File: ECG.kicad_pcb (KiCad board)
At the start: 2 copper layers, 50 x 50 mm, 84 parts, among them J1 SJ-3566AN, J2 Conn_01x02_Male, Q1 MMBT3904-7-F, U1 ADR4525, U2 SP6641, U3 INA333, U4 OPA388, U5 OPA388, U6 OPA388, U7 ADS1015IDGS

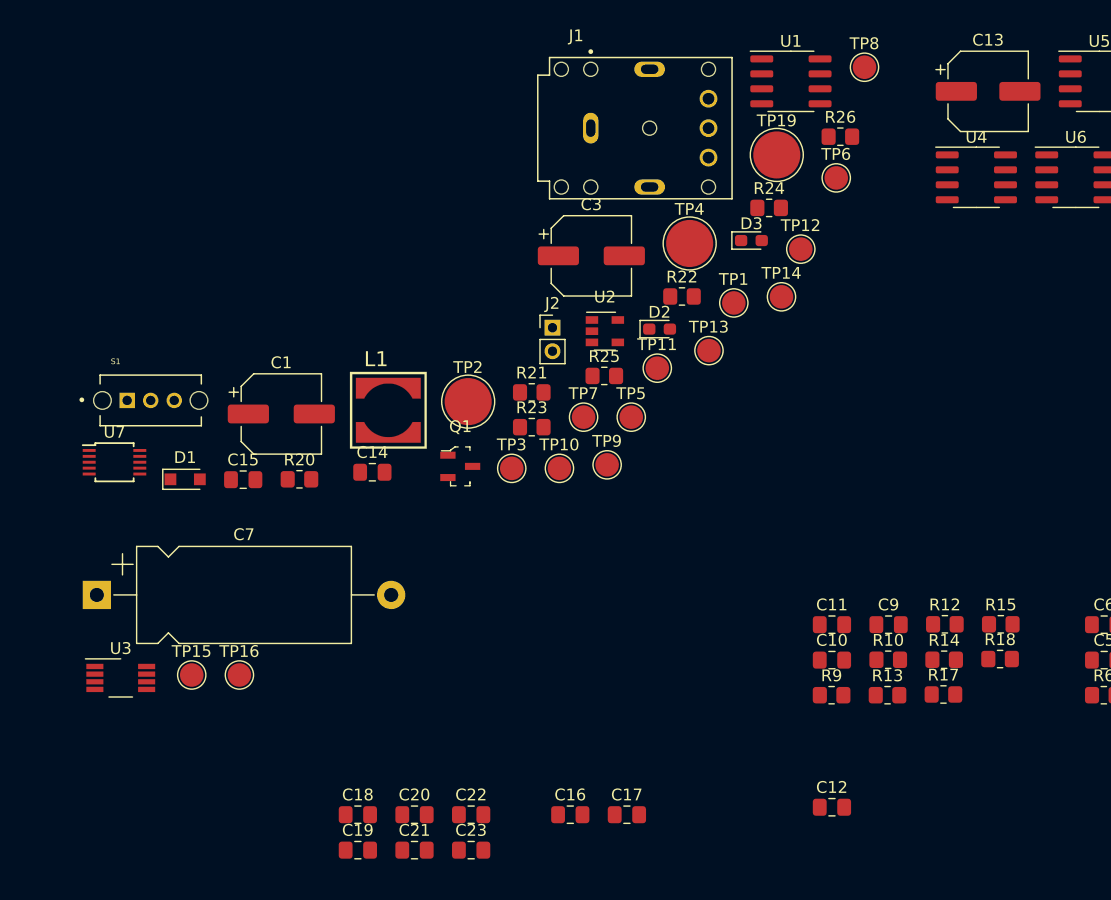
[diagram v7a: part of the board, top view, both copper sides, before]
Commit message: Removed extra caps and removed the tantalum cap as it was too large
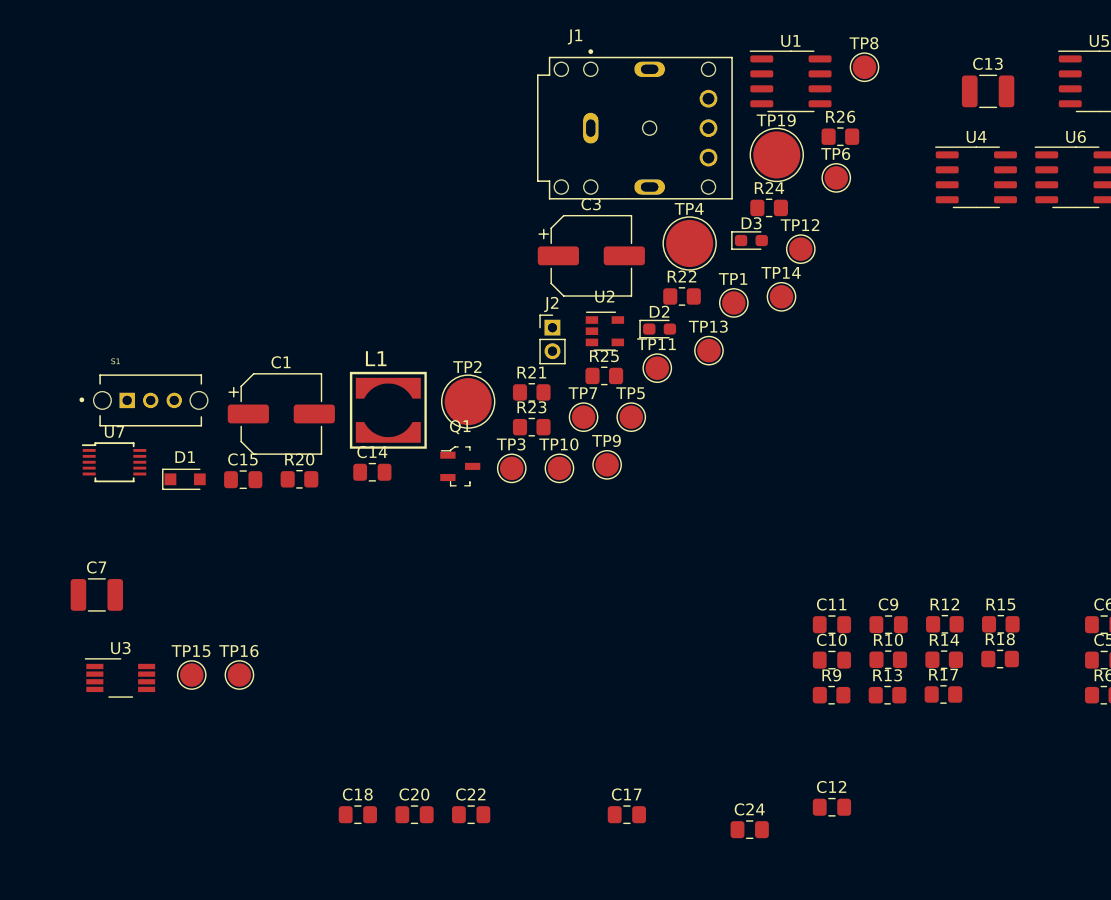
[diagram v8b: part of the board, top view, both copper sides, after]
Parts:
- removed C16, C19, C21, C23: 100n, Capacitor_SMD:C_0805_2012Metric_Pad1.18x1.45mm_HandSolder
- added C24: 100n, Capacitor_SMD:C_0805_2012Metric_Pad1.18x1.45mm_HandSolder, F.Cu at (192.4, 126.4)
- C13: footprint Capacitor_SMD:CP_Elec_6.3x3 -> Capacitor_SMD:C_1210_3225Metric_Pad1.33x2.70mm_HandSolder
- C7: footprint Capacitor_THT:CP_Axial_L18.0mm_D8.0mm_P25.00mm_Horizontal -> Capacitor_SMD:C_1210_3225Metric_Pad1.33x2.70mm_HandSolder
